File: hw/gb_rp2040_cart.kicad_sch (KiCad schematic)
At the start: 33 parts, among them J1 GameBoy_Cartridge, J2 DEBUG, U1 74VHC9164FT, U2 74LVC8T245PW, U3 74LVC8T245PW, U4 SN74AUP1T34DCK, U5 SN74AUP1T34DCK, U6 SN74AUP1T34DCK, U7 SN74AUP1T34DCK

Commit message: hw: start PCB layout
Signed-off-by: Mahyar Koshkouei <mk@deltabeard.com>
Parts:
- removed J?: Micro_SD_Card, symbol Connector:Micro_SD_Card
- removed U1: 74VHC9164FT, Package_SO:TSSOP-16_4.4x5mm_P0.65mm, symbol 74xx:74VHC9164FT
- added BT1: MS920SE, Project_Specific:BatteryHolder_Seiko_MS920SE, symbol Device:Battery_Cell
- added C10, C11, C12, C13, C14, C15, C17, C6, C7: 100n, Capacitor_SMD:C_0603_1608Metric, symbol Device:C_Small
- added C2, C3: 8p, Capacitor_SMD:C_0603_1608Metric, symbol Device:C_Small
- added C8, C9: 2.2u, Capacitor_SMD:C_0603_1608Metric, symbol Device:C_Small
- added D1: D_Schottky, Diode_SMD:D_0603_1608Metric, symbol Device:D_Schottky
- added R10, R11: 5k1, Resistor_SMD:R_0603_1608Metric, symbol Device:R_Small
- added R3: 600R, Resistor_SMD:R_0805_2012Metric, symbol Device:R_Small
- added TP1: MFP, TestPoint:TestPoint_THTPad_D2.0mm_Drill1.0mm, symbol Connector:TestPoint
- added U3: 74LVC8T245PW, Package_SO:TSSOP-24_4.4x7.8mm_P0.65mm, symbol Gekkio_Logic_LevelTranslator:74LVC8T245PW
- added U8: MCP7940N-xMNY, Package_DFN_QFN:DFN-8-1EP_3x2mm_P0.5mm_EP1.36x1.46mm, symbol Timer_RTC:MCP7940N-xMNY
- added Y1: 32.768k, Crystal:Crystal_SMD_5032-2Pin_5.0x3.2mm, symbol Device:Crystal_Small
- C16, C4, C5: renamed from C?; footprint (none) -> Capacitor_SMD:C_0603_1608Metric
- C18: renamed from C?; footprint (none) -> Capacitor_SMD:C_0805_2012Metric
- D2: renamed from D?; footprint (none) -> Diode_SMD:D_0603_1608Metric; MFr (none) -> 1SS417CT
- J1: footprint Gekkio_Connector_PCBEdge:GameBoy_Cartridge_1x32_P1.50mm_Edge -> Gekkio_Connector_PCBEdge:GameBoy_Cartridge_1x32_P1.50mm_Full
- J2: renamed from J?; footprint (none) -> Connector_USB:USB_C_Receptacle_XKB_U262-16XN-4BVC11
- J3: renamed from J?; footprint (none) -> Button_Switch_SMD:SW_SPST_B3U-1000P
- J4: renamed from J2; footprint Connector_PinSocket_2.54mm:PinSocket_1x03_P2.54mm_Vertical_SMD_Pin1Left -> Connector_PinSocket_2.54mm:PinSocket_1x03_P2.54mm_Horizontal
- L1: renamed from L?; footprint (none) -> Inductor_SMD:L_0805_2012Metric; MFr (none) -> MLZ2012N1R0LT000
- R1, R2, R4, R5, R6, R7, R8, R9: renamed from R?; footprint (none) -> Resistor_SMD:R_0603_1608Metric
- SW1: renamed from SW?; footprint (none) -> Button_Switch_SMD:SW_SPST_B3U-1000P
- U10: renamed from U?; footprint RP2040_minimal:RP2040-QFN-56 -> RP_RP2040:RP2040-QFN-56; MFr (none) -> RP2040
- U11: renamed from U?; footprint (none) -> Package_CSP:WLCSP-6_1.4x1.0mm_P0.4mm
- U9: renamed from U?; value W25Q128JVS -> W25Q128JVSIM
- Y2: renamed from Y?; footprint (none) -> Crystal:Crystal_SMD_TXC_7A-2Pin_5x3.2mm
- gave numbers to parts that had none: 1
- renumbered U4 to U1, U5 to U2, U2 to U4, U3 to U5
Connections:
- net LSB_ADDR_SERIAL is gone; now on net 3V3_A12: U10.31 (GPIO20)
- net SCK is gone; now on net 3V3_A14: U10.34 (GPIO22)
- net ~{SEL_LOW_ADDR} is gone; now on net 3V3_A13: U10.32 (GPIO21)
- net +3V3: now also C1.2, U10.1 (IOVDD), U10.10 (IOVDD), U10.22 (IOVDD), U10.33 (IOVDD), U10.42 (IOVDD), U10.43 (ADC_AVDD), U10.44 (VREG_IN), U10.48 (USB_VDD), U10.49 (IOVDD), C10.1, C11.1, C12.1, C13.1, C14.1, C15.1, C17.1, C9.1, D1.2 (A), R10.1, R11.1, U3.23 (VCC(B)), U3.24 (VCC(B)), U8.8 (VCC); no longer C1.1
- net +5V: now also U3.1 (VCC(A)), U3.2 (DIR)
- net 3V3_A10: now also U10.29 (GPIO18); no longer U10.13 (GPIO10)
- net 3V3_A11: now also U10.30 (GPIO19); no longer U10.14 (GPIO11)
- net 3V3_A12: no longer U10.15 (GPIO12)
- net 3V3_A13: no longer U10.16 (GPIO13)
- net 3V3_A14: no longer U10.17 (GPIO14)
- net 3V3_A15: now also U10.35 (GPIO23); no longer U10.18 (GPIO15)
- net 3V3_A8: now also U10.27 (GPIO16); no longer U10.11 (GPIO8)
- net 3V3_A9: now also U10.28 (GPIO17); no longer U10.12 (GPIO9)
- net A0: now also U3.3 (A1)
- net A1: now also U3.4 (A2)
- net A2: now also U3.5 (A3)
- net A3: now also U3.6 (A4)
- net A4: now also U3.7 (A5)
- net A5: now also U3.8 (A6)
- net A6: now also U3.9 (A7)
- net A7: now also U3.10 (A8)
- net GND: now also C1.1, BT1.2 (-), C10.2, C11.2, C12.2, C13.2, C14.2, C15.2, C17.2, C2.2, C3.1, C6.2, C7.2, C8.2, C9.2, U3.11 (GND), U3.12 (GND), U3.13 (GND), U3.22 (~{OE}), U8.4 (VSS), U8.9 (EP); no longer C1.2
- net PHI_3V3: now also U10.38 (GPIO26_ADC0); no longer U10.27 (GPIO16)
- net ~{CS}_3V3: now also U10.41 (GPIO29_ADC3); no longer U10.30 (GPIO19)
- net ~{RD}_3V3: now also U10.40 (GPIO28_ADC2); no longer U10.29 (GPIO18)
- net ~{WR}_3V3: now also U10.39 (GPIO27_ADC1); no longer U10.28 (GPIO17)
- net +1V1: now reaches U10.23 (DVDD)
- net +1V1: now also U10.45 (VREG_VOUT), U10.50 (DVDD), C6.1, C7.1, C8.1
- net I2C_SDA: now reaches U10.36 (GPIO24)
- net I2C_SDA: now also R10.2, U8.5 (SDA)
- net I2C_SCL: now reaches U10.37 (GPIO25)
- net I2C_SCL: now also R11.2, U8.6 (SCL)
- new net: D1.1 (K), R3.1
- new net: C2.1, U8.1 (X1), Y1.1
- new net: C3.2, U8.2 (X2), Y1.2
- new net: TP1.1, U8.7 (MFP)
- new net 3V3_A0: U10.11 (GPIO8), U3.21 (B1)
- new net 3V3_A1: U10.12 (GPIO9), U3.20 (B2)
- new net 3V3_A2: U10.13 (GPIO10), U3.19 (B3)
- new net 3V3_A3: U10.14 (GPIO11), U3.18 (B4)
- new net 3V3_A4: U10.15 (GPIO12), U3.17 (B5)
- new net 3V3_A5: U10.16 (GPIO13), U3.16 (B6)
- new net 3V3_A6: U10.17 (GPIO14), U3.15 (B7)
- new net 3V3_A7: U10.18 (GPIO15), U3.14 (B8)
- new net VBAT: BT1.1 (+), R3.2, U8.3 (VBAT)
- no-connect marks 7 -> 4
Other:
- note added: "Charging limited to 3.1V, 2mA."
- note added: "Cl=(Cx/2)+5"
- note added: "Cx=6-9pF"
- note added: "Logic level translation"
- note added: "Real Time Clock with backup cell"
- note added: "Use USB power if that is connected. Diode Vf <= 1.5"
- note added: "Vf >= 200mV"
- note removed: "Or SN74HCS165"
- note removed: "Shift register is 5V tolerant"
- note removed: "Use USB power if that is connected. The voltage drop over doide doesn't matter."
- moved on the sheet: C16, C18, C4, C5, D2, J1, J2, J3, J4, L1, Q1, R1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

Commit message: hw: finish layout
Signed-off-by: Mahyar Koshkouei <mk@deltabeard.com>
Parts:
- removed J2: USB_C_Receptacle_USB2.0, Connector_USB:USB_C_Receptacle_XKB_U262-16XN-4BVC11, symbol Connector:USB_C_Receptacle_USB2.0
- removed U1, U2, U6, U7: SN74AUP1T34DCK, Package_TO_SOT_SMD:SOT-353_SC-70-5, symbol Logic_LevelTranslator:SN74AUP1T34DCK
- removed U3, U4, U5: 74LVC8T245PW, Package_SO:TSSOP-24_4.4x7.8mm_P0.65mm, symbol Gekkio_Logic_LevelTranslator:74LVC8T245PW
- added C19, C20, C21, C22, C23, C24, C25, C26, C27: 100n, Capacitor_SMD:C_0603_1608Metric, symbol Device:C_Small
- added IC1, IC2, IC3: CLXC8T245QRHLRQ1, Project_Specific:CLXC8T245QRHLRQ1, symbol SamacSys_Parts:CLXC8T245QRHLRQ1
- added J2: USB4105-GF-A, Project_Specific:GCT_USB4105-GF-A, symbol USB4105-GF-A:USB4105-GF-A
- added J5: Expansion, Connector_PinSocket_2.54mm:PinSocket_1x04_P2.54mm_Horizontal, symbol Connector:Conn_01x04_Female
- added Q2: RU1J002YN, Package_TO_SOT_SMD:SOT-323_SC-70, symbol Device:Q_NMOS_GSD
- added TP2, TP3, TP4: MFP, TestPoint:TestPoint_Pad_D1.0mm, symbol Connector:TestPoint
- added U1: TXU0104, Package_SO:TSSOP-14_4.4x5mm_P0.65mm, symbol Project_specific:TXU0104
- added U12: PCA9536D, Package_SO:SOIC-8_3.9x4.9mm_P1.27mm, symbol Interface_Expansion:PCA9536D
- R3: value 600R -> 1k
- TP1: footprint TestPoint:TestPoint_THTPad_D2.0mm_Drill1.0mm -> TestPoint:TestPoint_Pad_D1.5mm
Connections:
- net +3V3: now also C22.2, C23.1, C25.2, C26.2, C27.2, IC1.23 (VCCB), IC1.24 (VCCB), IC2.23 (VCCB), IC2.24 (VCCB), IC3.23 (VCCB), IC3.24 (VCCB), J5.1 (Pin_1), U1.11 (VCC(B)), U1.12 (~{OE}), U12.8 (VDD)
- net +5V: now also C19.1, C20.1, C21.1, C24.1, IC1.1 (VCCA), IC2.1 (VCCA), IC2.2 (DIR), IC3.1 (VCCA), IC3.2 (DIR), U1.1 (VCC(A))
- net 3V3_A0: now also IC3.21 (B1)
- net 3V3_A1: now also IC3.20 (B2)
- net 3V3_A10: now also IC2.19 (B3)
- net 3V3_A11: now also IC2.18 (B4)
- net 3V3_A12: now also IC2.17 (B5)
- net 3V3_A13: now also IC2.16 (B6)
- net 3V3_A14: now also IC2.15 (B7)
- net 3V3_A15: now also IC2.14 (B8)
- net 3V3_A2: now also IC3.19 (B3)
- net 3V3_A3: now also IC3.18 (B4)
- net 3V3_A4: now also IC3.17 (B5)
- net 3V3_A5: now also IC3.16 (B6)
- net 3V3_A6: now also IC3.15 (B7)
- net 3V3_A7: now also IC3.14 (B8)
- net 3V3_A8: now also IC2.21 (B1)
- net 3V3_A9: now also IC2.20 (B2)
- net 3V3_D0: now also IC1.21 (B1)
- net 3V3_D1: now also IC1.20 (B2)
- net 3V3_D2: now also IC1.19 (B3)
- net 3V3_D3: now also IC1.18 (B4)
- net 3V3_D4: now also IC1.17 (B5)
- net 3V3_D5: now also IC1.16 (B6)
- net 3V3_D6: now also IC1.15 (B7)
- net 3V3_D7: now also IC1.14 (B8)
- net A0: now also IC3.3 (A1)
- net A1: now also IC3.4 (A2)
- net A10: now also IC2.5 (A3)
- net A11: now also IC2.6 (A4)
- net A12: now also IC2.7 (A5)
- net A13: now also IC2.8 (A6)
- net A14: now also IC2.9 (A7)
- net A15: now also IC2.10 (A8)
- net A2: now also IC3.5 (A3)
- net A3: now also IC3.6 (A4)
- net A4: now also IC3.7 (A5)
- net A5: now also IC3.8 (A6)
- net A6: now also IC3.9 (A7)
- net A7: now also IC3.10 (A8)
- net A8: now also IC2.3 (A1)
- net A9: now also IC2.4 (A2)
- net D0: now also IC1.3 (A1)
- net D1: now also IC1.4 (A2)
- net D2: now also IC1.5 (A3)
- net D3: now also IC1.6 (A4)
- net D4: now also IC1.7 (A5)
- net D5: now also IC1.8 (A6)
- net D6: now also IC1.9 (A7)
- net D7: now also IC1.10 (A8)
- net GND: now also C19.2, C20.2, C21.2, C22.1, C23.2, C24.2, C25.1, C26.1, C27.1, IC1.11 (GND), IC1.12 (GND), IC1.13 (GND), IC1.22 (~{OE}), IC1.25 (EP_1), IC1.A25 (EP_2), IC1.B25 (EP_3), IC1.C25 (EP_4), IC1.D25 (EP_5), IC1.E25 (EP_6), IC1.F25 (EP_7), IC2.11 (GND), IC2.12 (GND), IC2.13 (GND), IC2.22 (~{OE}), IC2.25 (EP_1), IC2.A25 (EP_2), IC2.B25 (EP_3), IC2.C25 (EP_4), IC2.D25 (EP_5), IC2.E25 (EP_6), IC2.F25 (EP_7), IC3.11 (GND), IC3.12 (GND), IC3.13 (GND), IC3.22 (~{OE}), IC3.25 (EP_1), IC3.A25 (EP_2), IC3.B25 (EP_3), IC3.C25 (EP_4), IC3.D25 (EP_5), IC3.E25 (EP_6), IC3.F25 (EP_7), J2.A1_B12 (GND), J2.B1_A12 (GND), J2.S1 (SHELL), J2.S2 (SHELL), J2.S3 (SHELL), J2.S4 (SHELL), J5.3 (Pin_3), Q2.2 (S), U1.6 (GND), U12.4 (VSS)
- net I2C_SCL: now also J5.4 (Pin_4), U12.6 (SCL)
- net I2C_SDA: now also J5.2 (Pin_2), U12.7 (SDA)
- net PHI: now also U1.2 (A1)
- net PHI_3V3: now also U1.10 (B1)
- net USB_DM: now also J2.A7 (DN1), J2.B7 (DN2)
- net USB_DP: now also J2.A6 (DP1), J2.B6 (DP2)
- net VBUS: now also J2.A4_B9 (VBUS), J2.B4_A9 (VBUS)
- net ~{CS}: now also U1.6 (GND)
- net ~{CS}_3V3: now also U1.7 (B4)
- net ~{RD}: now also IC1.2 (DIR), U1.4 (A3)
- net ~{RD}_3V3: now also U1.8 (B3)
- net ~{WR}: now also U1.3 (A2)
- net ~{WR}_3V3: now also U1.9 (B2)
- net at R2.2: now also J2.B5 (CC2)
- net at R4.1: now also J2.A5 (CC1)
- net ~{RES}: now reaches J1.30 (~{RES})
- net ~{RES}: now also Q2.3 (D)
- new net: TP2.1, U12.2 (IO1)
- new net: TP3.1, U12.3 (IO2)
- new net: TP4.1, U12.5 (IO3)
- new net RESET_GB: Q2.1 (G), U12.1 (IO0)
- no-connect marks 4 -> 3
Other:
- note added: "3.3V Power supply"
- note added: "I/O Expander Only use: reset the Game Boy."
- company: (none) -> Mahyar Koshkouei
- title: (none) -> RP2040 Game Boy Cart
- moved on the sheet: BT1, C1, C10, C11, C12, C13, C14, C15, C16, C17, C18, C2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

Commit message: Finish routing & final checks
Signed-off-by: Mahyar Koshkouei <mk@deltabeard.com>
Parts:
- removed D2: D_Schottky, Diode_SMD:D_0603_1608Metric, symbol Device:D_Schottky
- removed Q1: Si2319CDS, Package_TO_SOT_SMD:SOT-23, symbol Transistor_FET:Si2319CDS
- added C28, C29: 100n, Capacitor_SMD:C_0603_1608Metric, symbol Device:C_Small
- added R12: 1k, Resistor_SMD:R_0603_1608Metric, symbol Device:R_Small
- added U2: TPS2115, Package_SO:TSSOP-8_4.4x3mm_P0.65mm, symbol Project_specific:TPS2115
- R9: value 10k -> 1k
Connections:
- net +3V3: now also U1.14 (VCC(B)), U1.8 (~{OE}); no longer U1.11 (VCC(B)), U1.12 (~{OE})
- net +5V: now also U2.7 (OUT)
- net GB_5V: now also C29.2, U2.6 (IN2)
- net GND: now also R9.1, U1.7 (GND), C28.1, C29.1, R12.1, U2.3 (D1), U2.5 (GND); no longer R9.2, U1.6 (GND)
- net PHI_3V3: now also U1.13 (B1); no longer U1.10 (B1)
- net VBUS: now also C28.2, U2.8 (IN1); no longer R9.1
- net ~{CS}: now also U1.5 (A4); no longer U1.6 (GND)
- net ~{CS}_3V3: now also U1.10 (B4); no longer U1.7 (B4)
- net ~{RD}_3V3: now also U1.11 (B3); no longer U1.8 (B3)
- net ~{WR}_3V3: now also U1.12 (B2); no longer U1.9 (B2)
- net USB_DM renamed USB_DN
- new net: R12.2, R9.2, U2.4 (ILIM)
- no-connect marks 3 -> 5
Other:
- note added: "Use USB power if it is connected."
- note removed: "Use USB power if that is connected. Diode Vf <= 1.5"

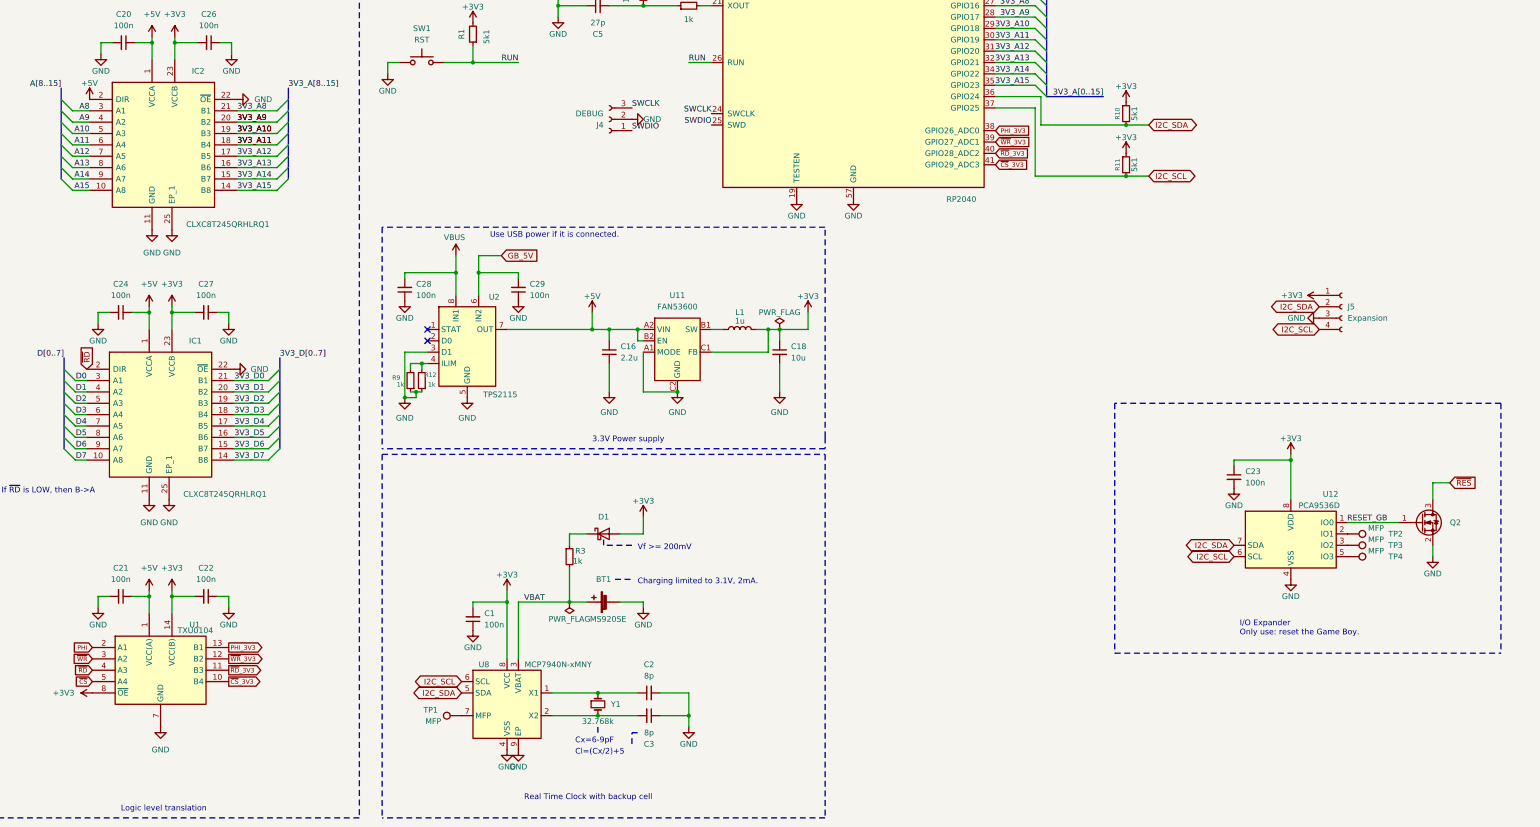
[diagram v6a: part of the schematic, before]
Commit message: hw: add fix for data direction
Signed-off-by: Mahyar Koshkouei <mk@deltabeard.com>
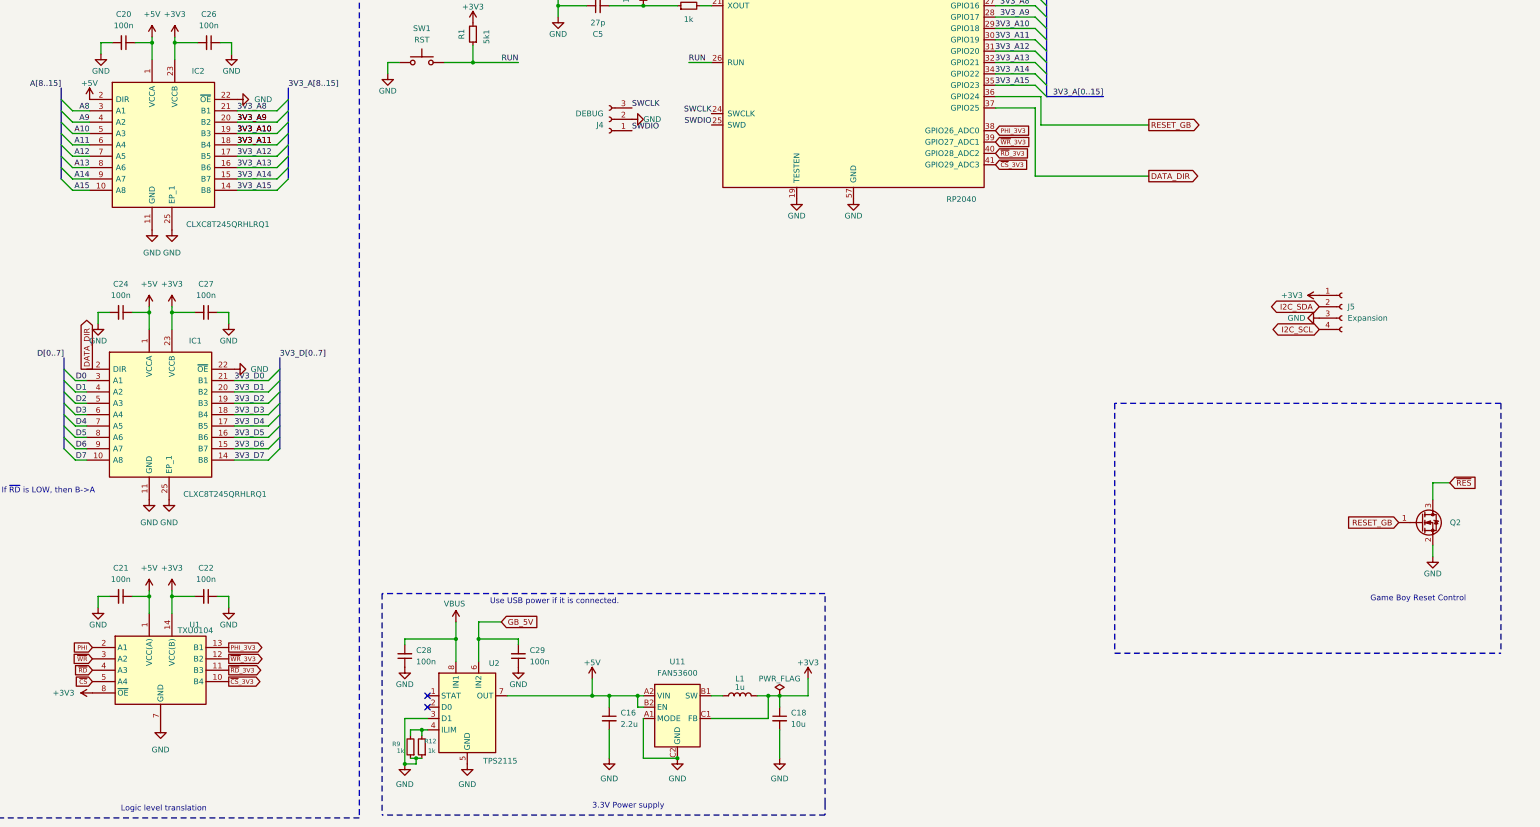
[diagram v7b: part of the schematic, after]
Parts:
- removed BT1: MS920SE, Project_Specific:BatteryHolder_Seiko_MS920SE, symbol Device:Battery_Cell
- removed C1, C23: 100n, Capacitor_SMD:C_0603_1608Metric, symbol Device:C_Small
- removed C2, C3: 8p, Capacitor_SMD:C_0603_1608Metric, symbol Device:C_Small
- removed D1: D_Schottky, Diode_SMD:D_0603_1608Metric, symbol Device:D_Schottky
- removed R10, R11: 5k1, Resistor_SMD:R_0603_1608Metric, symbol Device:R_Small
- removed R3: 1k, Resistor_SMD:R_0805_2012Metric, symbol Device:R_Small
- removed TP1: MFP, TestPoint:TestPoint_Pad_D1.5mm, symbol Connector:TestPoint
- removed TP2, TP3, TP4: MFP, TestPoint:TestPoint_Pad_D1.0mm, symbol Connector:TestPoint
- removed U12: PCA9536D, Package_SO:SOIC-8_3.9x4.9mm_P1.27mm, symbol Interface_Expansion:PCA9536D
- removed U8: MCP7940N-xMNY, Package_DFN_QFN:DFN-8-1EP_3x2mm_P0.5mm_EP1.36x1.46mm, symbol Timer_RTC:MCP7940N-xMNY
- removed Y1: 32.768k, Crystal:Crystal_SMD_5032-2Pin_5.0x3.2mm, symbol Device:Crystal_Small
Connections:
- net I2C_SCL: no longer U10.37 (GPIO25)
- net I2C_SDA: no longer U10.36 (GPIO24)
- net RESET_GB: now also U10.36 (GPIO24)
- net ~{RD}: no longer IC1.2 (DIR)
- new net DATA_DIR: IC1.2 (DIR), U10.37 (GPIO25)
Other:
- note added: "Game Boy Reset Control"
- note removed: "Charging limited to 3.1V, 2mA."
- note removed: "Cl=(Cx/2)+5"
- note removed: "Cx=6-9pF"
- note removed: "I/O Expander Only use: reset the Game Boy."
- note removed: "Real Time Clock with backup cell"
- note removed: "Vf >= 200mV"
- moved on the sheet: C16, C18, C28, C29, L1, R12, R9, U11, U2
